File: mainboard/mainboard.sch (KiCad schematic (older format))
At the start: 108 parts, among them J1 USB_B_Micro, J2 Conn_01x02_MountingPin, J3 Conn_01x19_MountingPin, J4 Conn_01x19_MountingPin, Q1 DMG2301L, Q2 MMBT3904, Q3 MMBT3904, SW1 SW_Push, SW2 SW_Push, U1 tps63070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

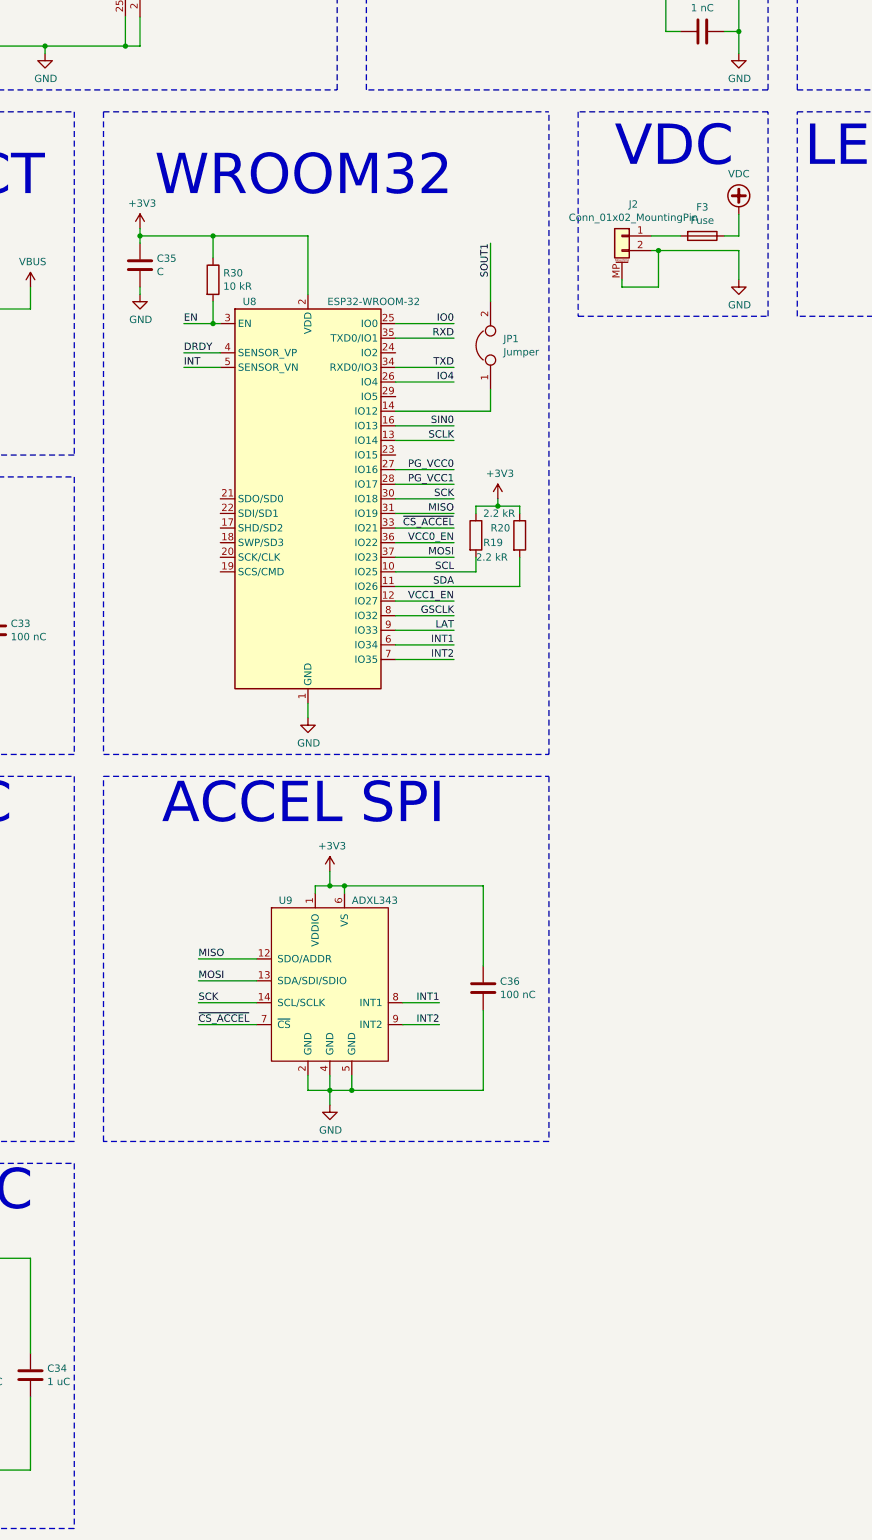
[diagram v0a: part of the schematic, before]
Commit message: Add VDC voltage measurement divider
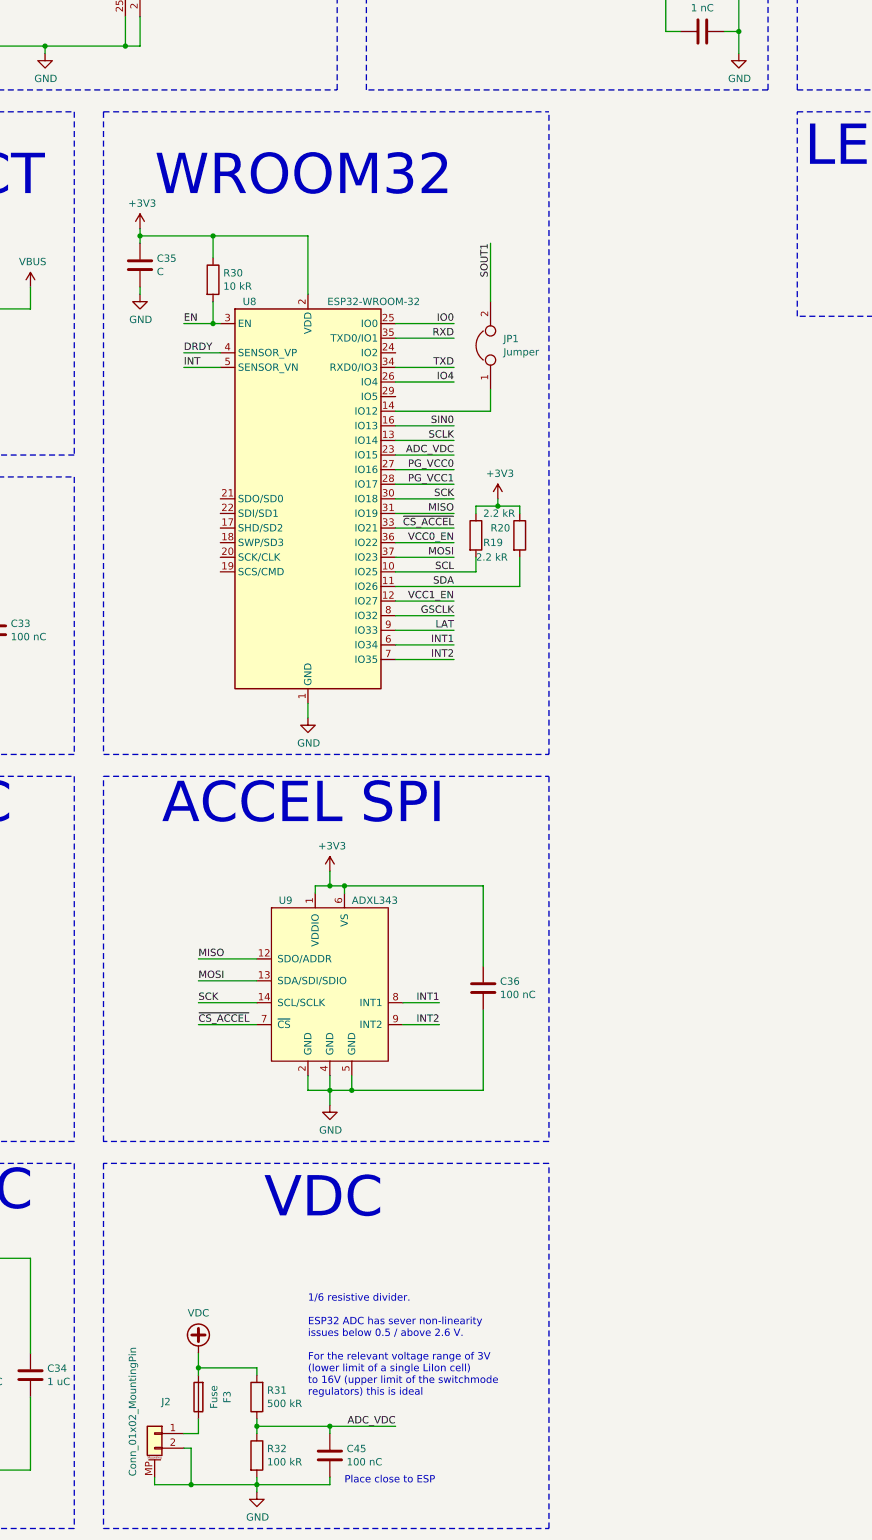
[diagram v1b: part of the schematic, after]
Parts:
- added C45: 100 nC, Capacitor_SMD:C_0805_2012Metric, symbol Device:C
- added R31: 500 kR, Resistor_SMD:R_0805_2012Metric, symbol Device:R
- added R32: 100 kR, Resistor_SMD:R_0805_2012Metric, symbol Device:R
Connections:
- net GND: now also C45.2, R32.2
- net VDC: now also F3.2, R31.2; no longer F3.1
- net ADC_VDC: now reaches U8.23 (IO15)
- net ADC_VDC: now also C45.1, R31.1, R32.1
- net at J2.1 (Pin_1): now also F3.1; no longer F3.2
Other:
- note added: "1/6 resistive divider.\n\nESP32 ADC has sever non-linearity\nissues below 0.5 / above 2.6 V.\n\nFor the relevant voltage range of 3V\n(lower limit of a single LiIon cell)\nto 16V (upper limit of the switchmode\nregulators) this is ideal"
- note added: "Place close to ESP\n"
- moved on the sheet: F3, J2
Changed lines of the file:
@@
 L power:VDC #PWR032
 U 1 1 5DF194F2
-P 14550 4600
-F 0 "#PWR032" H 14550 4500 50  0001 C CNN
-F 1 "VDC" H 14550 4875 50  0000 C CNN
-F 2 "" H 14550 4600 50  0001 C CNN
-F 3 "" H 14550 4600 50  0001 C CNN
-	1    14550 4600
+P 10850 12400
+F 0 "#PWR032" H 10850 12300 50  0001 C CNN
+F 1 "VDC" H 10850 12675 50  0000 C CNN
+F 2 "" H 10850 12400 50  0001 C CNN
+F 3 "" H 10850 12400 50  0001 C CNN
+	1    10850 12400
 	1    0    0    -1
 $EndComp
@@
 L Device:Fuse F3
 U 1 1 5DF1A160
-P 14300 4750
-F 0 "F3" V 14103 4750 50  0000 C CNN
-F 1 "Fuse" V 14194 4750 50  0000 C CNN
-F 2 "Fuse:Fuse_1206_3216Metric" V 14230 4750 50  0001 C CNN
-F 3 "~" H 14300 4750 50  0001 C CNN
-	1    14300 4750
-	0    1    1    0
-$EndComp
-Wire Wire Line
-	14450 4750 14550 4750
-Wire Wire Line
-	14550 4750 14550 4600
-Wire Wire Line
-	13950 4750 14150 4750
+P 10850 12700
+F 0 "F3" V 10653 12700 50  0000 C CNN
+F 1 "Fuse" V 10744 12700 50  0000 C CNN
+F 2 "Fuse:Fuse_1206_3216Metric" V 10780 12700 50  0001 C CNN
+F 3 "~" H 10850 12700 50  0001 C CNN
+	1    10850 12700
+	-1   0    0    1
+$EndComp
 $Comp
 L power:GND #PWR033
 U 1 1 5DFF9B28
-P 14550 5050
-F 0 "#PWR033" H 14550 4800 50  0001 C CNN
-F 1 "GND" H 14555 4877 50  0000 C CNN
-F 2 "" H 14550 5050 50  0001 C CNN
-F 3 "" H 14550 5050 50  0001 C CNN
-	1    14550 5050
-	1    0    0    -1
-$EndComp
-Wire Wire Line
-	14550 5050 14550 4850
-Wire Wire Line
-	14550 4850 14000 4850
-Wire Notes Line
-	13450 3900 13450 5300
-Wire Notes Line
-	13450 5300 14750 5300
-Wire Notes Line
-	14750 5300 14750 3900
-Wire Notes Line
-	14750 3900 13450 3900
-Text Notes 13700 4300 0    276  ~ 0
+P 11250 13350
+F 0 "#PWR033" H 11250 13100 50  0001 C CNN
+F 1 "GND" H 11255 13177 50  0000 C CNN
+F 2 "" H 11250 13350 50  0001 C CNN
+F 3 "" H 11250 13350 50  0001 C CNN
+	1    11250 13350
+	1    0    0    -1
+$EndComp
+Text Notes 11300 11500 0    276  ~ 0
 VDC
 Wire Wire Line
@@
 L Connector_Generic_MountingPin:Conn_01x02_MountingPin J2
 U 1 1 5F516B43
-P 13750 4750
-F 0 "J2" H 13672 4967 50  0000 C CNN
-F 1 "Conn_01x02_MountingPin" H 13672 4876 50  0000 C CNN
-F 2 "mainboard:XT30PW" H 13750 4750 50  0001 C CNN
-F 3 "~" H 13750 4750 50  0001 C CNN
-	1    13750 4750
+P 10550 12950
+F 0 "J2" H 10472 13167 50  0000 C CNN
+F 1 "Conn_01x02_MountingPin" V 10700 13100 50  0000 C CNN
+F 2 "mainboard:XT30PW" H 10550 12950 50  0001 C CNN
+F 3 "~" H 10550 12950 50  0001 C CNN
+	1    10550 12950
 	-1   0    0    -1
 $EndComp
 Wire Wire Line
-	13750 5050 13750 5100
-Wire Wire Line
-	13750 5100 14000 5100
-Wire Wire Line
-	14000 5100 14000 4850
-Connection ~ 14000 4850
-Wire Wire Line
-	14000 4850 13950 4850
+	10550 13250 10550 13300
+Wire Wire Line
+	10550 13300 10800 13300
+Wire Wire Line
+	10800 13300 10800 13050
+Wire Wire Line
+	10800 13050 10750 13050
 Connection ~ 14550 3350
 Wire Wire Line
@@
 Wire Wire Line
 	10950 4750 10450 4750
+Wire Wire Line
+	12200 6250 12600 6250
+Text Label 12600 6250 2    50   ~ 0
+ADC_VDC
+$Comp
+L Device:R R31
+U 1 1 5D64A05F
+P 11250 12700
+F 0 "R31" H 11180 12654 50  0000 R CNN
+F 1 "500 kR" H 11180 12745 50  0000 R CNN
+F 2 "Resistor_SMD:R_0805_2012Metric" V 11180 12700 50  0001 C CNN
+F 3 "~" H 11250 12700 50  0001 C CNN
+	1    11250 12700
+	-1   0    0    1
+$EndComp
+Wire Notes Line
+	10200 11100 10200 13600
+Wire Notes Line
+	10200 13600 13250 13600
+Wire Notes Line
+	13250 13600 13250 11100
+Wire Notes Line
+	13250 11100 10200 11100
+Wire Wire Line
+	10850 12550 10850 12500
+Wire Wire Line
+	10850 12950 10850 12850
+Wire Wire Line
+	10750 12950 10850 12950
+Connection ~ 10800 13300
+$Comp
+L Device:R R32
+U 1 1 5D8867DB
+P 11250 13100
+F 0 "R32" H 11320 13146 50  0000 L CNN
+F 1 "100 kR" H 11320 13055 50  0000 L CNN
+F 2 "Resistor_SMD:R_0805_2012Metric" V 11180 13100 50  0001 C CNN
+F 3 "~" H 11250 13100 50  0001 C CNN
+	1    11250 13100
+	1    0    0    -1
+$EndComp
+Wire Wire Line
+	11250 12950 11250 12900
+Wire Wire Line
+	11250 12550 11250 12500
+Wire Wire Line
+	11250 12500 10850 12500
+Connection ~ 10850 12500
+Wire Wire Line
+	10850 12500 10850 12400
+Wire Wire Line
+	11250 13250 11250 13300
+Wire Wire Line
+	10800 13300 11250 13300
+Wire Wire Line
+	11250 13350 11250 13300
+Connection ~ 11250 13300
+Connection ~ 11250 12900
+Wire Wire Line
+	11250 12900 11250 12850
+Text Label 12200 12900 2    50   ~ 0
+ADC_VDC
+Text Notes 11600 12700 0    50   ~ 0
+1/6 resistive divider.\n\nESP32 ADC has sever non-linearity\nissues below 0.5 / above 2.6 V.\n\nFor the relevant voltage range of 3V\n(lower limit of a single LiIon cell)\nto 16V (upper limit of the switchmode\nregulators) this is ideal
+$Comp
+L Device:C C45
+U 1 1 5DA89BF0
+P 11750 13100
+F 0 "C45" H 11865 13146 50  0000 L CNN
+F 1 "100 nC" H 11865 13055 50  0000 L CNN
+F 2 "Capacitor_SMD:C_0805_2012Metric" H 11788 12950 50  0001 C CNN
+F 3 "~" H 11750 13100 50  0001 C CNN
+	1    11750 13100
+	1    0    0    -1
+$EndComp
+Wire Wire Line
+	11750 12950 11750 12900
+Wire Wire Line
+	11250 12900 11750 12900
+Wire Wire Line
+	11750 12900 12200 12900
+Connection ~ 11750 12900
+Wire Wire Line
+	11750 13250 11750 13300
+Wire Wire Line
+	11750 13300 11250 13300
 Wire Bus Line
 	8350 2150 8350 2500
 Wire Bus Line
 	9350 2500 9350 2750
+Text Notes 11850 13300 0    50   ~ 0
+Place close to ESP\n
 $EndSCHEMATC

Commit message: Add pdm microphone
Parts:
- added C46: 100 nC, Capacitor_SMD:C_0805_2012Metric, symbol Device:C
- added U10: SPH064X, sph064x:SPH064X, symbol sph064x:SPH064X
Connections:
- net +3V3: now also C46.1, U10.2 (SELECT), U10.5 (VDD)
- net GND: now also C46.2, U10.3 (GND)
- net I2S_CLK: now reaches U8.24 (IO2)
- net I2S_CLK: now also U10.4 (CLOCK)
- net I2S_DATA: now reaches U8.29 (IO5)
- net I2S_DATA: now also U10.1 (DATA)
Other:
- note added: "MIC"
- moved on the sheet: C29, C32, C34, C45, D3, D4, D5, D6, D7, D8, D9, F3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

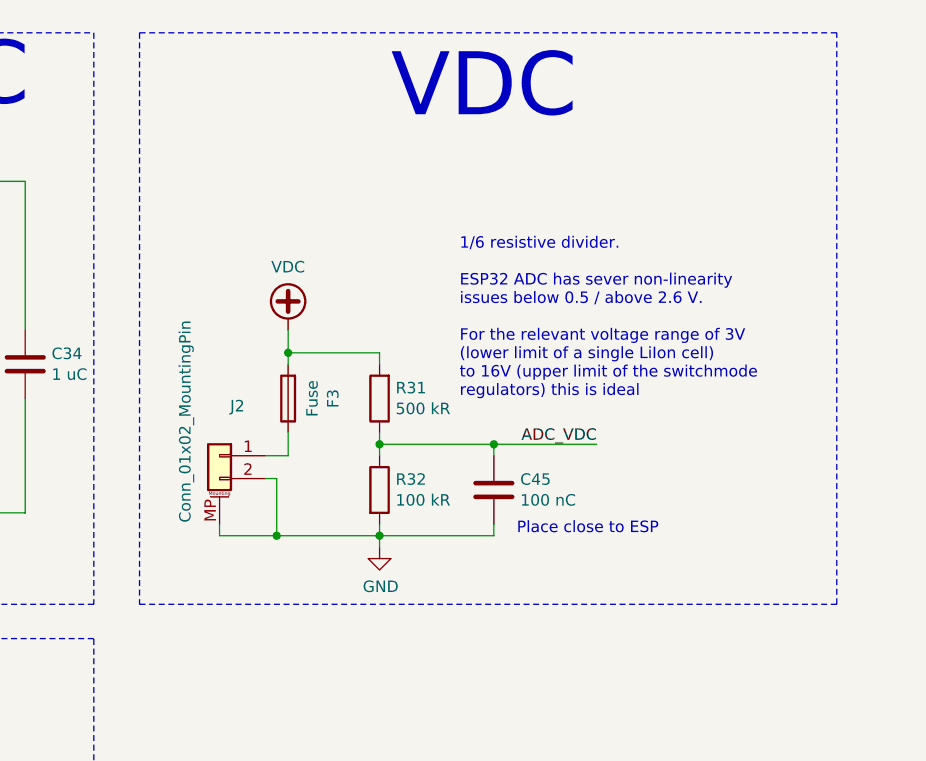
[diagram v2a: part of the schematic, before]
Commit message: Add VDC input protection
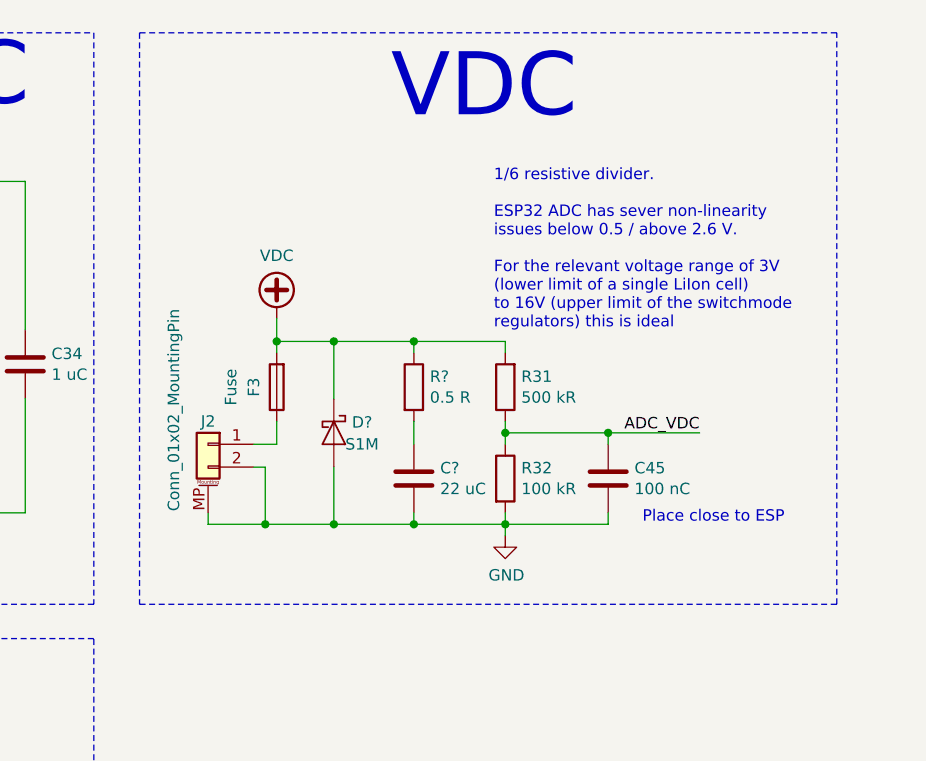
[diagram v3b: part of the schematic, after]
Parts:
- added C?: 22 uC, Capacitor_SMD:C_1210_3225Metric, symbol Device:C
- added D?: S1M, Diode_SMD:D_SMA, symbol Device:D_Schottky
- added R?: 0.5 R, Resistor_SMD:R_1210_3225Metric, symbol Device:R
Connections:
- net GND: now also C?.2, D?.2 (A)
- net VDC: now also D?.1 (K), R?.1
- new net: C?.1, R?.2
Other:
- moved on the sheet: C45, F3, J2, R31, R32
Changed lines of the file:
@@
 L power:VDC #PWR032
 U 1 1 5DF194F2
-P 19050 6750
-F 0 "#PWR032" H 19050 6650 50  0001 C CNN
-F 1 "VDC" H 19050 7025 50  0000 C CNN
-F 2 "" H 19050 6750 50  0001 C CNN
-F 3 "" H 19050 6750 50  0001 C CNN
-	1    19050 6750
+P 19000 6700
+F 0 "#PWR032" H 19000 6600 50  0001 C CNN
+F 1 "VDC" H 19000 6975 50  0000 C CNN
+F 2 "" H 19000 6700 50  0001 C CNN
+F 3 "" H 19000 6700 50  0001 C CNN
+	1    19000 6700
 	1    0    0    -1
 $EndComp
@@
 L Device:Fuse F3
 U 1 1 5DF1A160
-P 19050 7050
-F 0 "F3" V 18853 7050 50  0000 C CNN
-F 1 "Fuse" V 18944 7050 50  0000 C CNN
-F 2 "Fuse:Fuse_1206_3216Metric" V 18980 7050 50  0001 C CNN
-F 3 "~" H 19050 7050 50  0001 C CNN
-	1    19050 7050
+P 19000 7000
+F 0 "F3" V 19100 7000 50  0000 C CNN
+F 1 "Fuse" V 19200 7000 50  0000 C CNN
+F 2 "Fuse:Fuse_1206_3216Metric" V 18930 7000 50  0001 C CNN
+F 3 "~" H 19000 7000 50  0001 C CNN
+	1    19000 7000
 	-1   0    0    1
 $EndComp
@@
 L power:GND #PWR033
 U 1 1 5DFF9B28
-P 19450 7700
-F 0 "#PWR033" H 19450 7450 50  0001 C CNN
-F 1 "GND" H 19455 7527 50  0000 C CNN
-F 2 "" H 19450 7700 50  0001 C CNN
-F 3 "" H 19450 7700 50  0001 C CNN
-	1    19450 7700
+P 20000 7650
+F 0 "#PWR033" H 20000 7400 50  0001 C CNN
+F 1 "GND" H 20005 7477 50  0000 C CNN
+F 2 "" H 20000 7650 50  0001 C CNN
+F 3 "" H 20000 7650 50  0001 C CNN
+	1    20000 7650
 	1    0    0    -1
 $EndComp
@@
 L Connector_Generic_MountingPin:Conn_01x02_MountingPin J2
 U 1 1 5F516B43
-P 18750 7300
-F 0 "J2" H 18672 7517 50  0000 C CNN
-F 1 "Conn_01x02_MountingPin" V 18900 7450 50  0000 C CNN
-F 2 "mainboard:XT30PW" H 18750 7300 50  0001 C CNN
-F 3 "~" H 18750 7300 50  0001 C CNN
-	1    18750 7300
+P 18700 7250
+F 0 "J2" H 18700 7350 50  0000 C CNN
+F 1 "Conn_01x02_MountingPin" V 18850 7400 50  0000 C CNN
+F 2 "mainboard:XT30PW" H 18700 7250 50  0001 C CNN
+F 3 "~" H 18700 7250 50  0001 C CNN
+	1    18700 7250
 	-1   0    0    -1
 $EndComp
 Wire Wire Line
-	18750 7600 18750 7650
-Wire Wire Line
-	18750 7650 19000 7650
-Wire Wire Line
-	19000 7650 19000 7400
-Wire Wire Line
-	19000 7400 18950 7400
+	18700 7550 18700 7600
+Wire Wire Line
+	18700 7600 18950 7600
+Wire Wire Line
+	18950 7600 18950 7350
+Wire Wire Line
+	18950 7350 18900 7350
 Connection ~ 14550 3350
 Wire Wire Line
@@
 L Device:R R31
 U 1 1 5D64A05F
-P 19450 7050
-F 0 "R31" H 19380 7004 50  0000 R CNN
-F 1 "500 kR" H 19380 7095 50  0000 R CNN
-F 2 "Resistor_SMD:R_0805_2012Metric" V 19380 7050 50  0001 C CNN
-F 3 "~" H 19450 7050 50  0001 C CNN
-	1    19450 7050
+P 20000 7000
+F 0 "R31" H 19930 6954 50  0000 R CNN
+F 1 "500 kR" H 19930 7045 50  0000 R CNN
+F 2 "Resistor_SMD:R_0805_2012Metric" V 19930 7000 50  0001 C CNN
+F 3 "~" H 20000 7000 50  0001 C CNN
+	1    20000 7000
 	-1   0    0    1
 $EndComp
@@
 	21450 5450 18400 5450
 Wire Wire Line
-	19050 6900 19050 6850
-Wire Wire Line
-	19050 7300 19050 7200
-Wire Wire Line
-	18950 7300 19050 7300
-Connection ~ 19000 7650
+	19000 7250 19000 7150
+Wire Wire Line
+	18900 7250 19000 7250
 $Comp
 L Device:R R32
 U 1 1 5D8867DB
-P 19450 7450
-F 0 "R32" H 19520 7496 50  0000 L CNN
-F 1 "100 kR" H 19520 7405 50  0000 L CNN
-F 2 "Resistor_SMD:R_0805_2012Metric" V 19380 7450 50  0001 C CNN
-F 3 "~" H 19450 7450 50  0001 C CNN
-	1    19450 7450
-	1    0    0    -1
-$EndComp
-Wire Wire Line
-	19450 7300 19450 7250
-Wire Wire Line
-	19450 6900 19450 6850
-Wire Wire Line
-	19450 6850 19050 6850
-Connection ~ 19050 6850
-Wire Wire Line
-	19050 6850 19050 6750
-Wire Wire Line
-	19450 7600 19450 7650
-Wire Wire Line
-	19000 7650 19450 7650
-Wire Wire Line
-	19450 7700 19450 7650
-Connection ~ 19450 7650
-Connection ~ 19450 7250
-Wire Wire Line
-	19450 7250 19450 7200
-Text Label 20400 7250 2    50   ~ 0
+P 20000 7400
+F 0 "R32" H 20070 7446 50  0000 L CNN
+F 1 "100 kR" H 20070 7355 50  0000 L CNN
+F 2 "Resistor_SMD:R_0805_2012Metric" V 19930 7400 50  0001 C CNN
+F 3 "~" H 20000 7400 50  0001 C CNN
+	1    20000 7400
+	1    0    0    -1
+$EndComp
+Wire Wire Line
+	20000 7250 20000 7200
+Wire Wire Line
+	20000 6850 20000 6800
+Wire Wire Line
+	20000 7550 20000 7600
+Wire Wire Line
+	20000 7650 20000 7600
+Connection ~ 20000 7600
+Connection ~ 20000 7200
+Wire Wire Line
+	20000 7200 20000 7150
+Text Label 20850 7200 2    50   ~ 0
 ADC_VDC
-Text Notes 19800 7050 0    50   ~ 0
+Text Notes 19950 6750 0    50   ~ 0
 1/6 resistive divider.\n\nESP32 ADC has sever non-linearity\nissues below 0.5 / above 2.6 V.\n\nFor the relevant voltage range of 3V\n(lower limit of a single LiIon cell)\nto 16V (upper limit of the switchmode\nregulators) this is ideal
 $Comp
 L Device:C C45
 U 1 1 5DA89BF0
-P 19950 7450
-F 0 "C45" H 20065 7496 50  0000 L CNN
-F 1 "100 nC" H 20065 7405 50  0000 L CNN
-F 2 "Capacitor_SMD:C_0805_2012Metric" H 19988 7300 50  0001 C CNN
-F 3 "~" H 19950 7450 50  0001 C CNN
-	1    19950 7450
-	1    0    0    -1
-$EndComp
-Wire Wire Line
-	19950 7300 19950 7250
-Wire Wire Line
-	19450 7250 19950 7250
-Wire Wire Line
-	19950 7250 20400 7250
-Connection ~ 19950 7250
-Wire Wire Line
-	19950 7600 19950 7650
-Wire Wire Line
-	19950 7650 19450 7650
-Text Notes 20050 7650 0    50   ~ 0
+P 20450 7400
+F 0 "C45" H 20565 7446 50  0000 L CNN
+F 1 "100 nC" H 20565 7355 50  0000 L CNN
+F 2 "Capacitor_SMD:C_0805_2012Metric" H 20488 7250 50  0001 C CNN
+F 3 "~" H 20450 7400 50  0001 C CNN
+	1    20450 7400
+	1    0    0    -1
+$EndComp
+Text Notes 20600 7600 0    50   ~ 0
 Place close to ESP\n
 Wire Wire Line
@@
 Wire Wire Line
 	16550 8800 17050 8800
+Wire Wire Line
+	20000 7200 20450 7200
+Wire Wire Line
+	20000 7600 20450 7600
+Wire Wire Line
+	20450 7600 20450 7550
+Wire Wire Line
+	20450 7250 20450 7200
+Wire Wire Line
+	20850 7200 20450 7200
+Connection ~ 20450 7200
+Wire Wire Line
+	19000 6700 19000 6800
+Wire Wire Line
+	19000 6800 19250 6800
+Connection ~ 19000 6800
+Wire Wire Line
+	19000 6800 19000 6850
+Wire Wire Line
+	18950 7600 19250 7600
+Connection ~ 18950 7600
+$Comp
+L Device:R R?
+U 1 1 5E9DA20F
+P 19600 7000
+F 0 "R?" H 19670 7046 50  0000 L CNN
+F 1 "0.5 R" H 19670 6955 50  0000 L CNN
+F 2 "Resistor_SMD:R_1210_3225Metric" V 19530 7000 50  0001 C CNN
+F 3 "~" H 19600 7000 50  0001 C CNN
+	1    19600 7000
+	1    0    0    -1
+$EndComp
+$Comp
+L Device:C C?
+U 1 1 5EA32808
+P 19600 7400
+F 0 "C?" H 19715 7446 50  0000 L CNN
+F 1 "22 uC" H 19715 7355 50  0000 L CNN
+F 2 "Capacitor_SMD:C_1210_3225Metric" H 19638 7250 50  0001 C CNN
+F 3 "~" H 19600 7400 50  0001 C CNN
+	1    19600 7400
+	1    0    0    -1
+$EndComp
+Wire Wire Line
+	19600 7250 19600 7150
+Connection ~ 19250 6800
+Connection ~ 19250 7600
+Wire Wire Line
+	19250 7600 19600 7600
+Wire Wire Line
+	19250 6800 19600 6800
+Wire Wire Line
+	19600 6850 19600 6800
+Connection ~ 19600 6800
+Wire Wire Line
+	19600 6800 20000 6800
+Wire Wire Line
+	19600 7550 19600 7600
+Connection ~ 19600 7600
+Wire Wire Line
+	19600 7600 20000 7600
+$Comp
+L Device:D_Schottky D?
+U 1 1 5EC98730
+P 19250 7200
+F 0 "D?" V 19204 7279 50  0000 L CNN
+F 1 "S1M" V 19300 7250 50  0000 L CNN
+F 2 "Diode_SMD:D_SMA" H 19250 7200 50  0001 C CNN
+F 3 "~" H 19250 7200 50  0001 C CNN
+	1    19250 7200
+	0    1    1    0
+$EndComp
+Wire Wire Line
+	19250 6800 19250 7050
+Wire Wire Line
+	19250 7350 19250 7600
 Wire Bus Line
 	8350 2150 8350 2500
